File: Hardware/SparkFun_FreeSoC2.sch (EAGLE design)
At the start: 107 parts, among them U1 CY8C5888AXI-LP096, U2 MIC5219 5V, U3 MIC5219 3.3V, U4 2A/20V, U7 CY8C5868LTI-LP039, Y1 32.768kHz

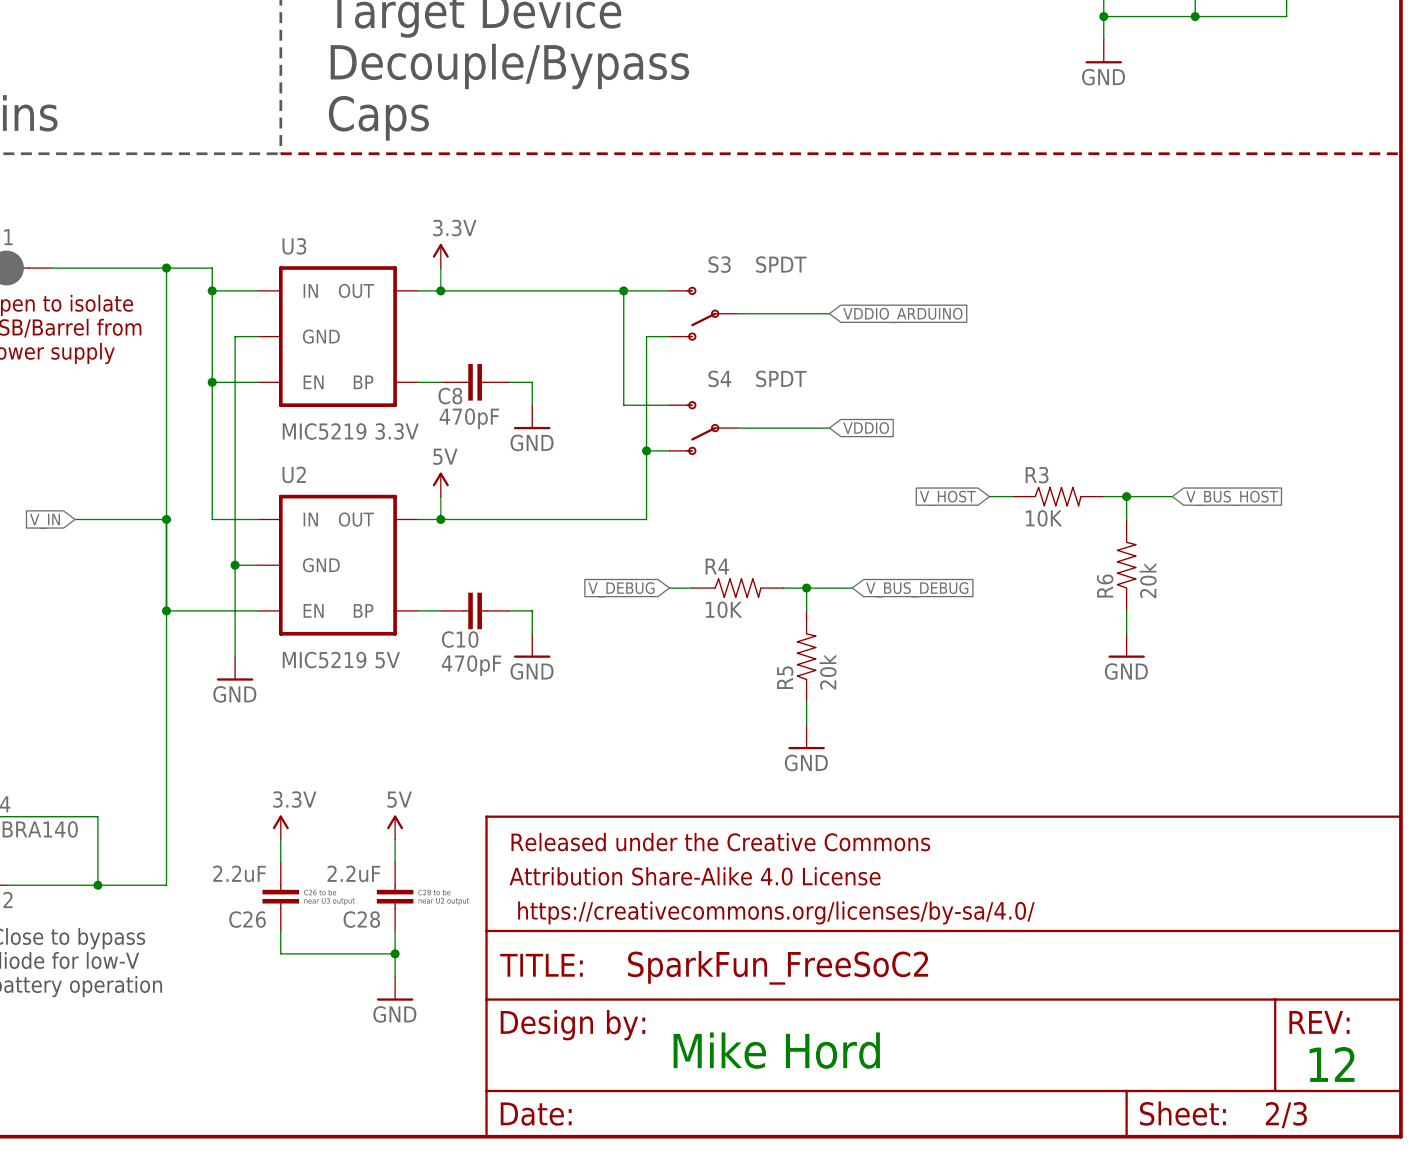
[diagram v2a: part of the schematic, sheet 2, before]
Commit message: Changes from user feedback and experience
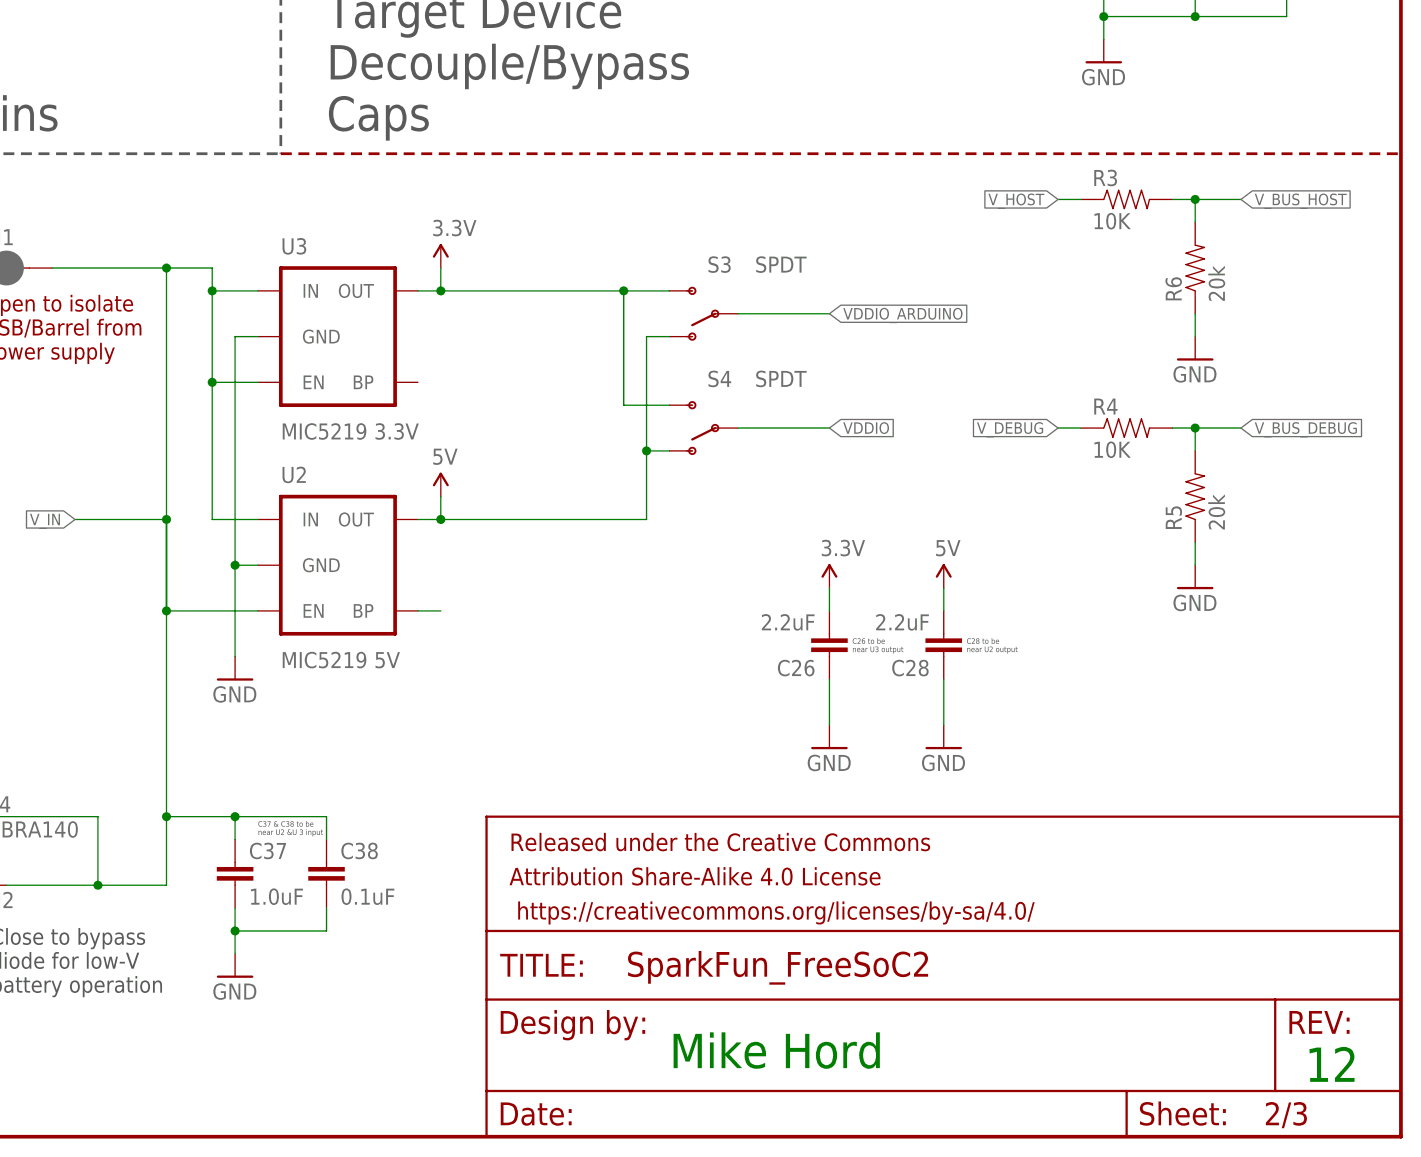
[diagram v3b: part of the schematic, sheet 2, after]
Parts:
- removed C10, C8: 470pF, SparkFun-Capacitors:470PF-50V-5%(0603)SMD
- added C37: 1.0uF, SparkFun-Capacitors:1.0UF-16V-10%(0603)
- added C38: 0.1uF, SparkFun-Capacitors:0.1UF-25V(+80/-20%)(0603)
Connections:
- removed net N$1: C8.1, U3.BP
- net GND: now also C37.2, C38.2; no longer C10.2, C8.2
- net N$2: no longer C10.1
- net V_IN: now also C37.1, C38.1
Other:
- note added: "C37 & C38 to be near U2 &U 3 input"
- moved on the sheet: C26, C28, R3, R4, R5, R6

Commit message: Enthickened lines on logos for better rendering
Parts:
- FRAME1, FRAME2, FRAME3: value (none) -> FRAME-LETTERNO_PACKAGE

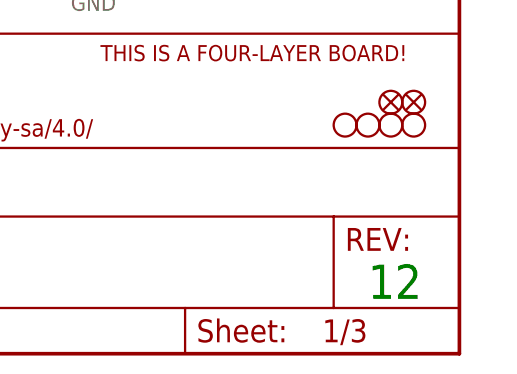
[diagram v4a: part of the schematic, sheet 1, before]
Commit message: Chg to V13, fix traces over vias
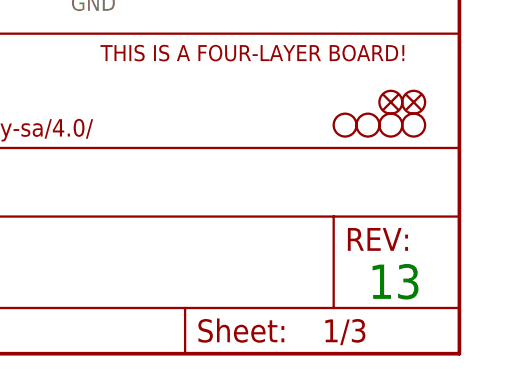
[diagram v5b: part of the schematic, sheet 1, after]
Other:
- note added: "13"
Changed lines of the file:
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@@
 LED</text>
 <text x="167.64" y="7.62" size="3.81" layer="91">Mike Hord</text>
-<text x="238.76" y="6.096" size="3.81" layer="91">12</text>
+<text x="238.76" y="6.096" size="3.81" layer="91">13</text>
 </plain>
 <instances>

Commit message: Advance v# on pgs 2 and 3
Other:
- note removed: "12"
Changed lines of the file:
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@@
 <text x="35.56" y="17.78" size="1.778" layer="97">JP3 is DNP</text>
 <text x="167.64" y="7.62" size="3.81" layer="91">Mike Hord</text>
-<text x="238.252" y="6.096" size="3.81" layer="91">12</text>
+<text x="238.252" y="6.096" size="3.81" layer="91">13</text>
 <text x="121.92" y="33.528" size="0.6096" layer="97">C37 &amp; C38 to be
 near U2 &amp;U 3 input</text>
@@
 to target via I2C</text>
 <text x="167.64" y="7.62" size="3.81" layer="91">Mike Hord</text>
-<text x="237.744" y="6.35" size="3.81" layer="91">12</text>
+<text x="237.744" y="6.35" size="3.81" layer="91">13</text>
 </plain>
 <instances>
